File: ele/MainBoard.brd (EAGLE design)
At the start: 136.6 x 100 mm, 114 parts, among them IC1 MCP23017SP, IC2 74HC595D, IC3 74HC595D, X1 POWER_IN, X2 POWER_OUT

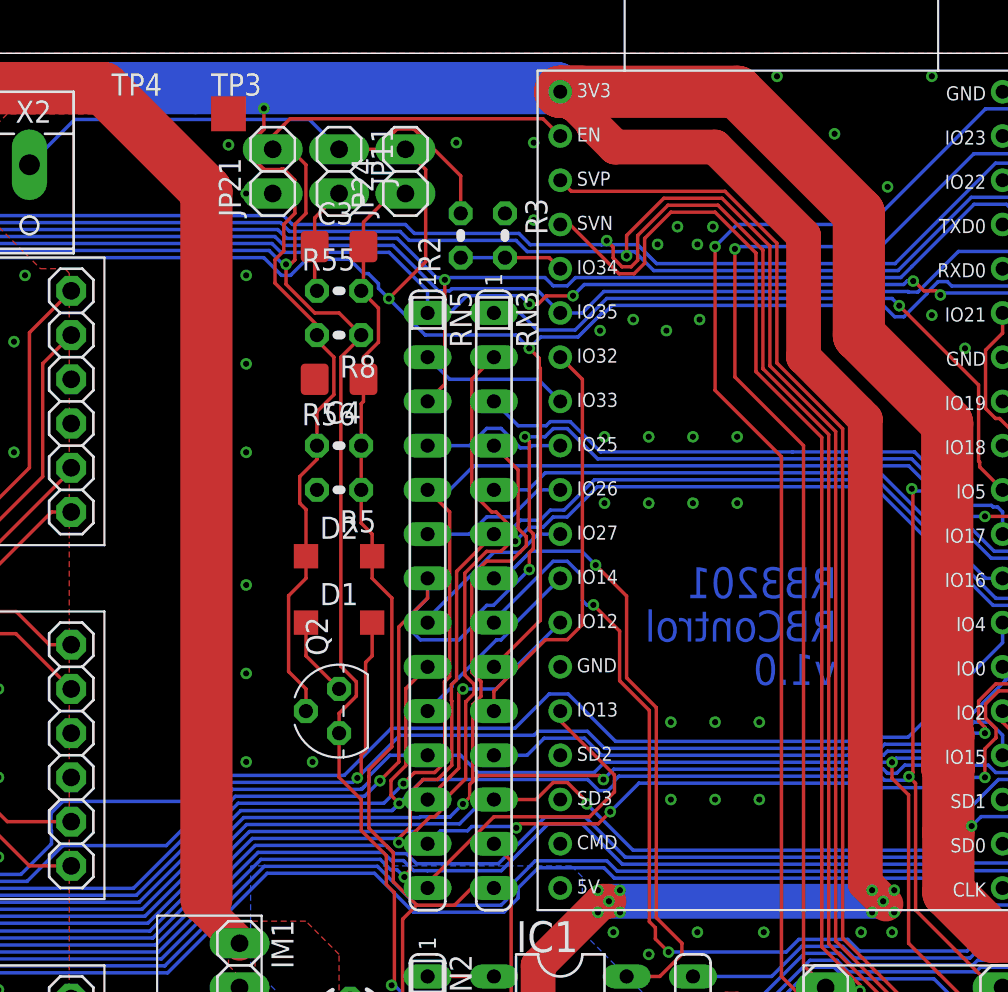
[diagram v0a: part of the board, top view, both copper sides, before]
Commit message: Add licenses to Eagle files
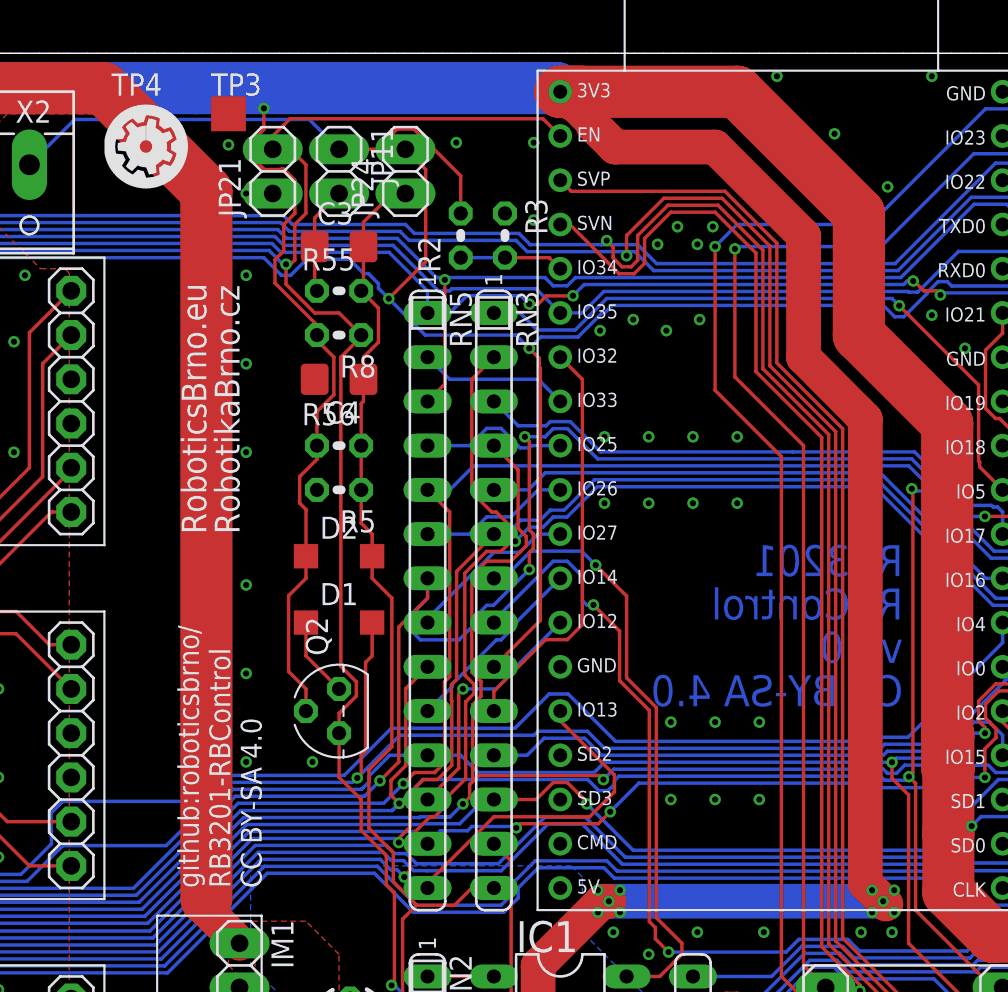
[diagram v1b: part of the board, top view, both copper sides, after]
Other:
- board text added: "RB3201 RBControl v1.0 CC BY-SA 4.0"
- board text added: "RoboticsBrno.eu"
- board text added: "RobotikaBrno.cz"
- board text added: "github:roboticsbrno/ RB3201-RBControl CC BY-SA 4.0"
- board text removed: "RB3201 RBControl v1.0"

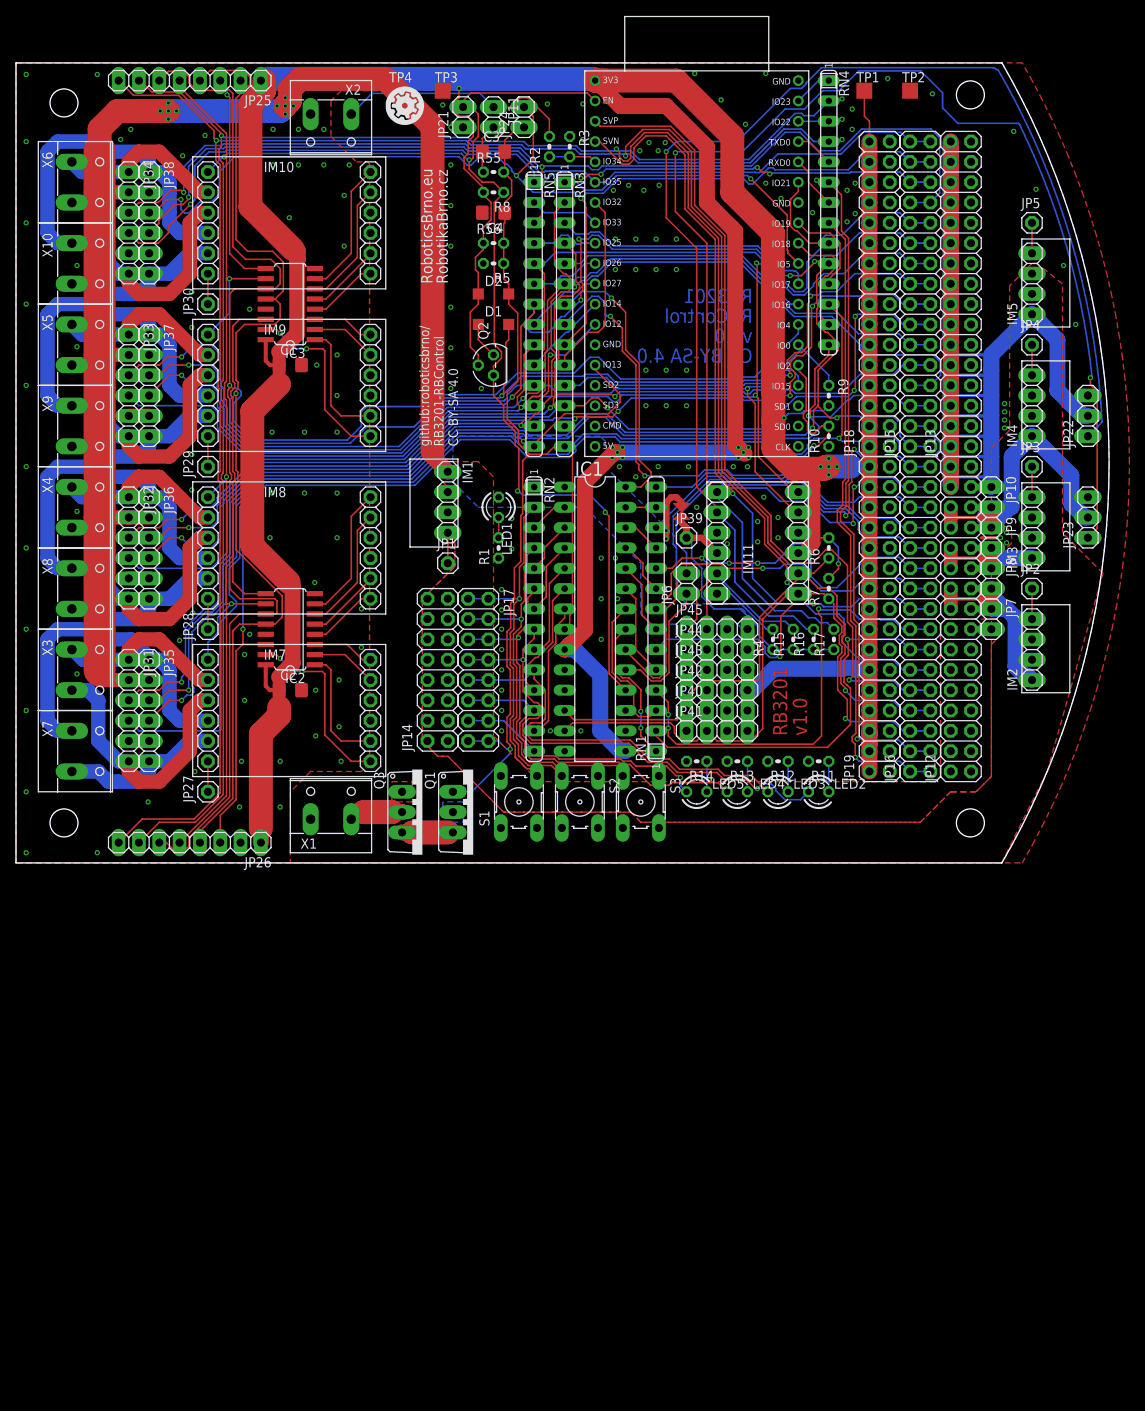
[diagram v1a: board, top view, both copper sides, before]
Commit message: ele: MainBoard - start work on v1.1 - make round corners (now just of left side)
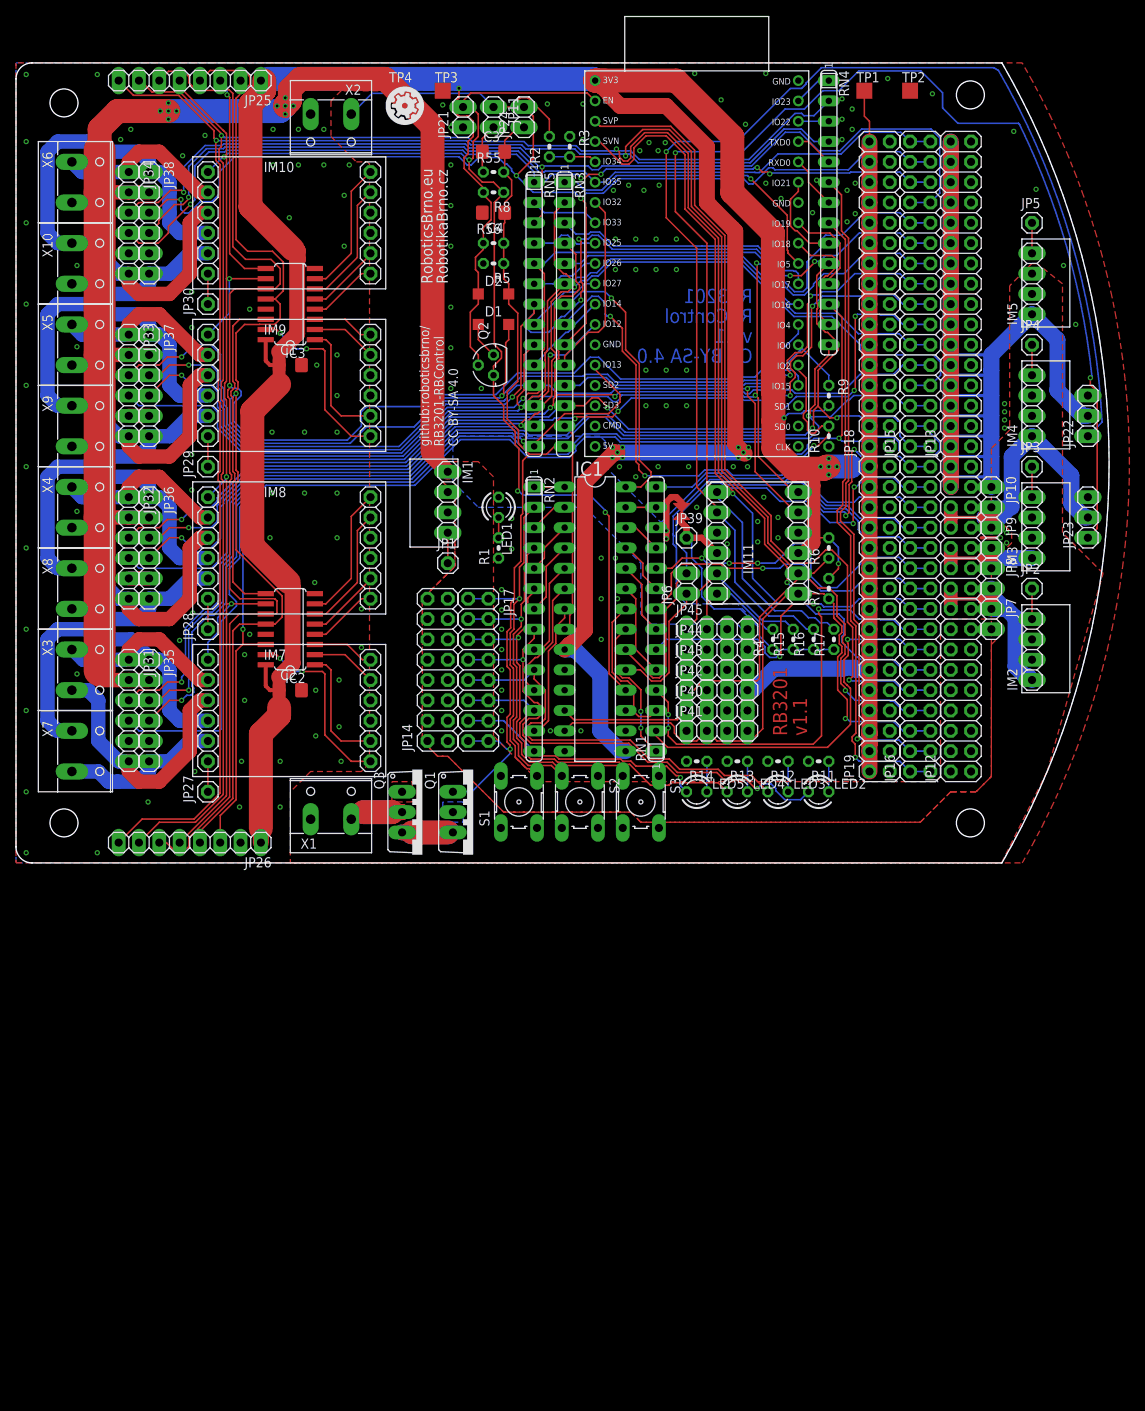
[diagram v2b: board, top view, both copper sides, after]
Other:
- outline, holes or cut-outs redrawn
- board text added: "RB3201 RBControl v1.1 CC BY-SA 4.0"
- board text added: "RB3201 v1.1"
- board text added: "RB3201-RBControl v1.1"
- board text removed: "RB3201 RBControl v1.0 CC BY-SA 4.0"
- board text removed: "RB3201 v1.0"
- board text removed: "RB3201-RBControl v1.0"
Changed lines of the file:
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@@
 <plain>
 <wire x1="123.24" y1="0" x2="123.24" y2="100" width="0" layer="20" curve="60"/>
-<wire x1="123.24" y1="100" x2="0" y2="100" width="0" layer="20"/>
-<wire x1="0" y1="100" x2="0" y2="0" width="0" layer="20"/>
-<wire x1="0" y1="0" x2="123.24" y2="0" width="0" layer="20"/>
+<wire x1="123.24" y1="100" x2="2" y2="100" width="0" layer="20"/>
+<wire x1="2" y1="100" x2="0" y2="98" width="0" layer="20" curve="90"/>
+<wire x1="0" y1="98" x2="0" y2="2" width="0" layer="20"/>
+<wire x1="0" y1="2" x2="2" y2="0" width="0" layer="20" curve="90"/>
+<wire x1="2" y1="0" x2="123.24" y2="0" width="0" layer="20"/>
 <hole x="6" y="5" drill="3.5"/>
 <hole x="6" y="95" drill="3.5"/>
@@
 <text x="115.714" y="9.779" size="1.5" layer="51" font="vector" ratio="20" rot="R270">5V</text>
 <text x="94.615" y="15.875" size="1.778" layer="1" font="vector" ratio="14" distance="40" rot="R90" align="top-left">RB3201
-v1.0</text>
+v1.1</text>
 <text x="121.048" y="26.035" size="1" layer="51" font="vector" ratio="20">A0</text>
 <text x="123.588" y="28.575" size="1" layer="51" font="vector" ratio="20">A1</text>
@@
 <text x="92.075" y="71.755" size="1.778" layer="16" font="vector" ratio="14" distance="40" rot="MR0" align="top-left">RB3201
 RBControl
-v1.0
+v1.1
 CC BY-SA 4.0</text>
-<text x="49.784" y="70.739" size="2.54" layer="51" font="vector" ratio="20" distance="40" rot="R90" align="bottom-center">RB3201-RBControl v1.0</text>
+<text x="49.784" y="70.739" size="2.54" layer="51" font="vector" ratio="20" distance="40" rot="R90" align="bottom-center">RB3201-RBControl v1.1</text>
 <text x="52.07" y="72.39" size="1.4224" layer="21" font="vector" ratio="20" rot="R90">RoboticsBrno.eu</text>
 <text x="55.245" y="52.07" size="1.2" layer="21" font="vector" ratio="16" rot="R90">github:roboticsbrno/

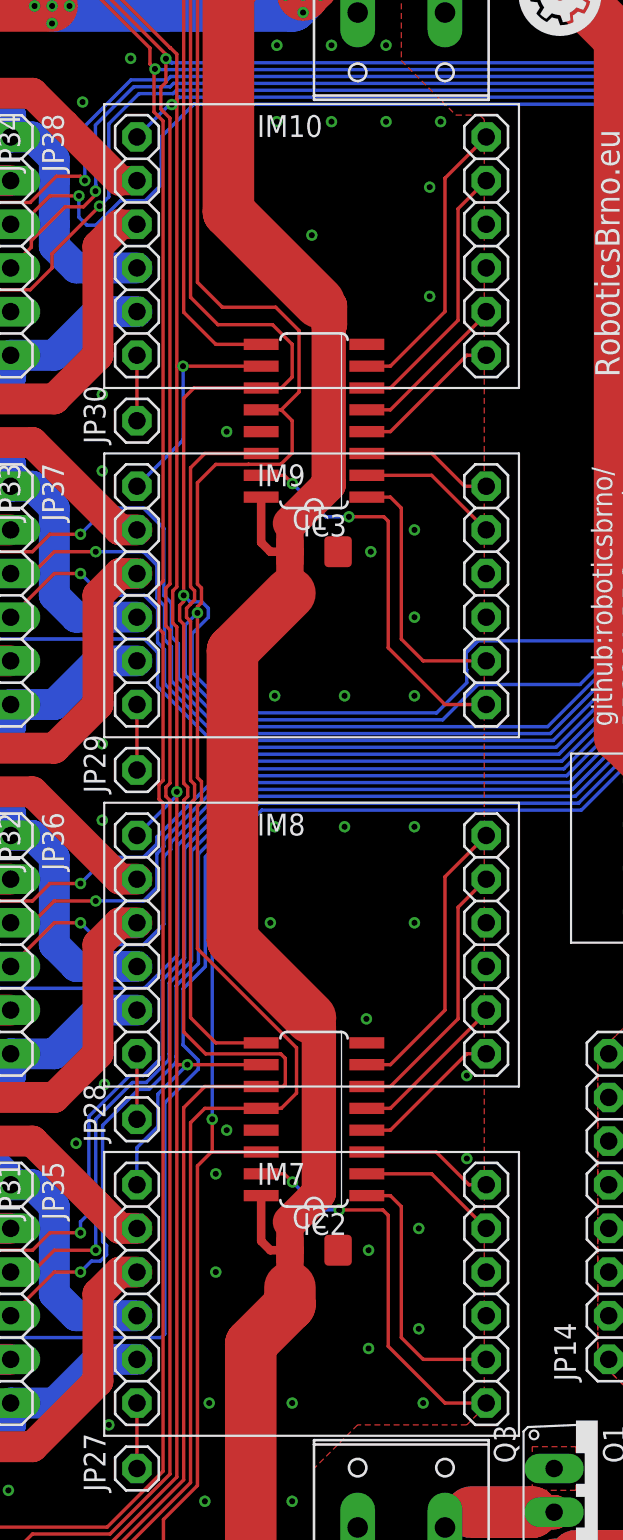
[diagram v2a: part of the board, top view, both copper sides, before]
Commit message: ele: Corrected DRV8833 pinhead package.
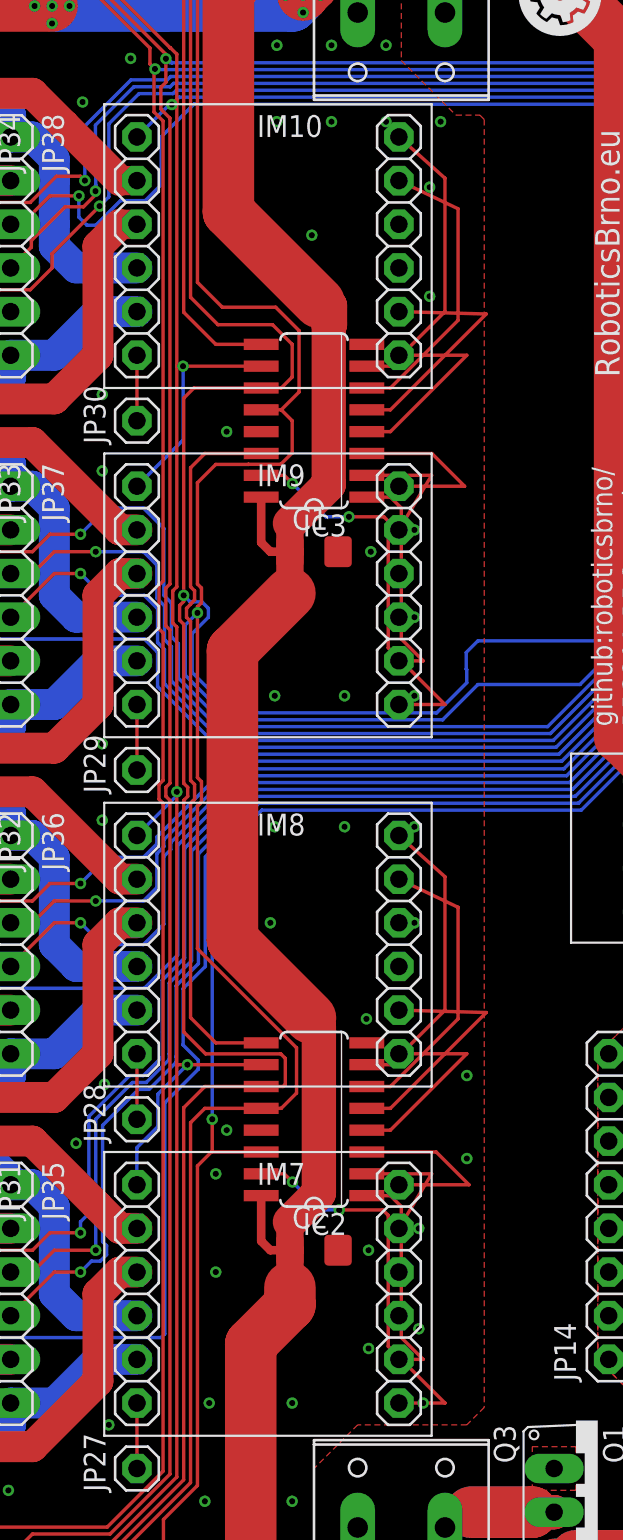
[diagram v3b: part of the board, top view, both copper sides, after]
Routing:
- net IC3_F: track 9.40 -> 14.3 mm
- net IC2_F: track 9.40 -> 14.3 mm
- net IC2_D: track 7.74 -> 10.8 mm
- net IC3_E: track 8.79 -> 11.6 mm
- net IC2_E: track 8.79 -> 11.6 mm
- net IC3_D: track 7.74 -> 10.3 mm
- net IC3_B: track 15.4 -> 13.1 mm
- net IC2_B: track 15.4 -> 13.1 mm
- net IC3_G: track 15.7 -> 17.2 mm
- net IC2_G: track 15.7 -> 17.2 mm
- net IC3_C: track 8.26 -> 7.47 mm
- net IC2_C: track 8.26 -> 7.47 mm
